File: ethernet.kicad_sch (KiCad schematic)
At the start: 3 parts, among them U1 MCIMX6Y2DVM09AB

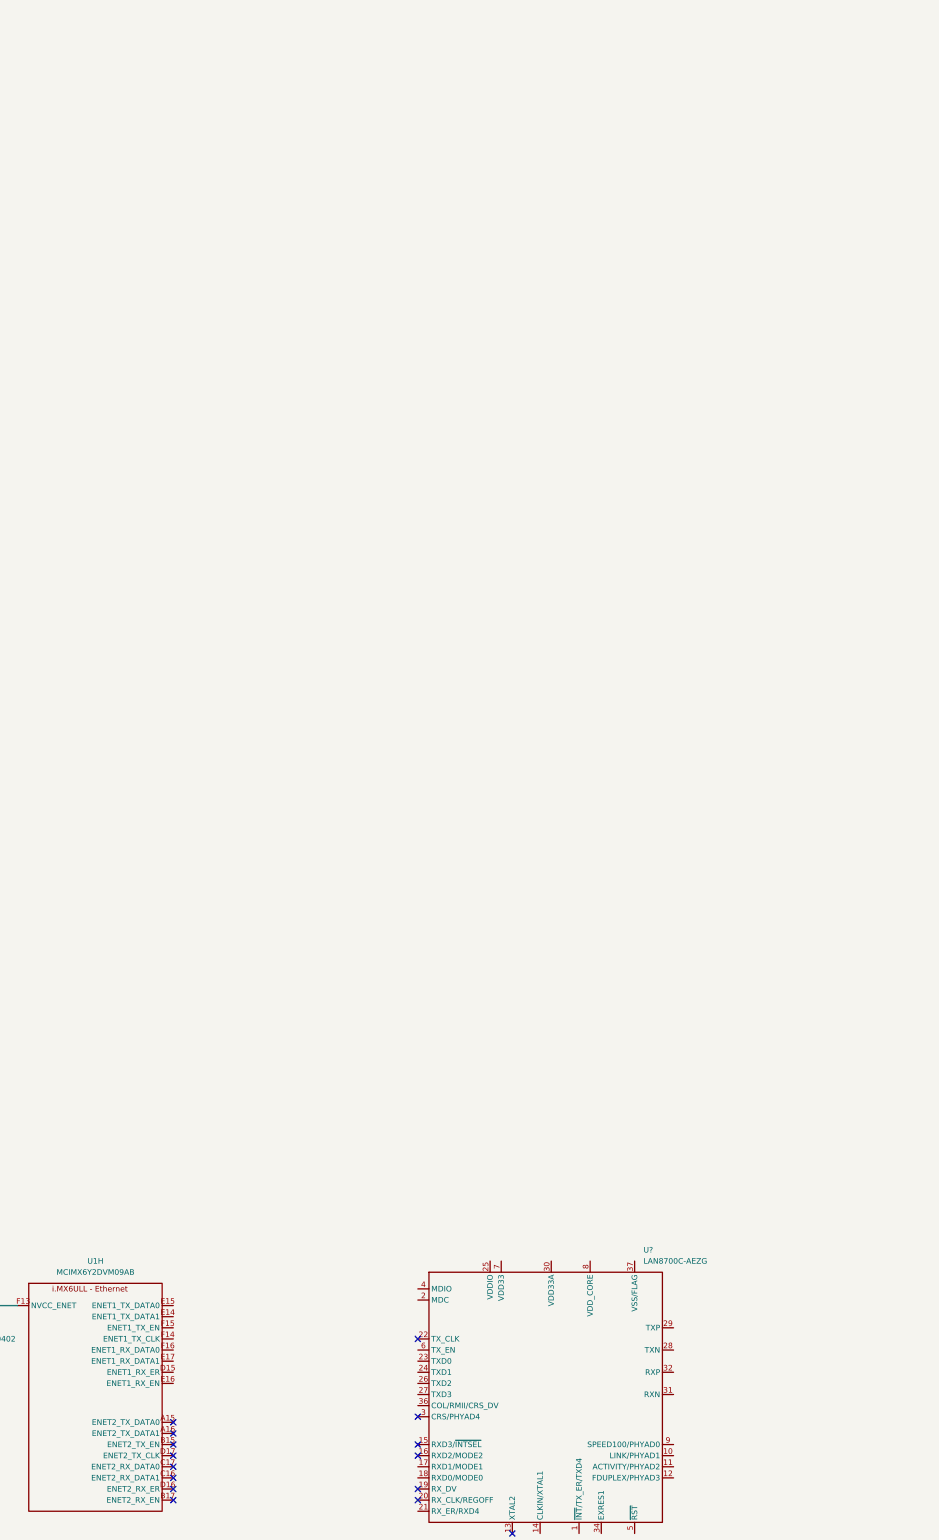
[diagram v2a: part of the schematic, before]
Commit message: H1102 symbol
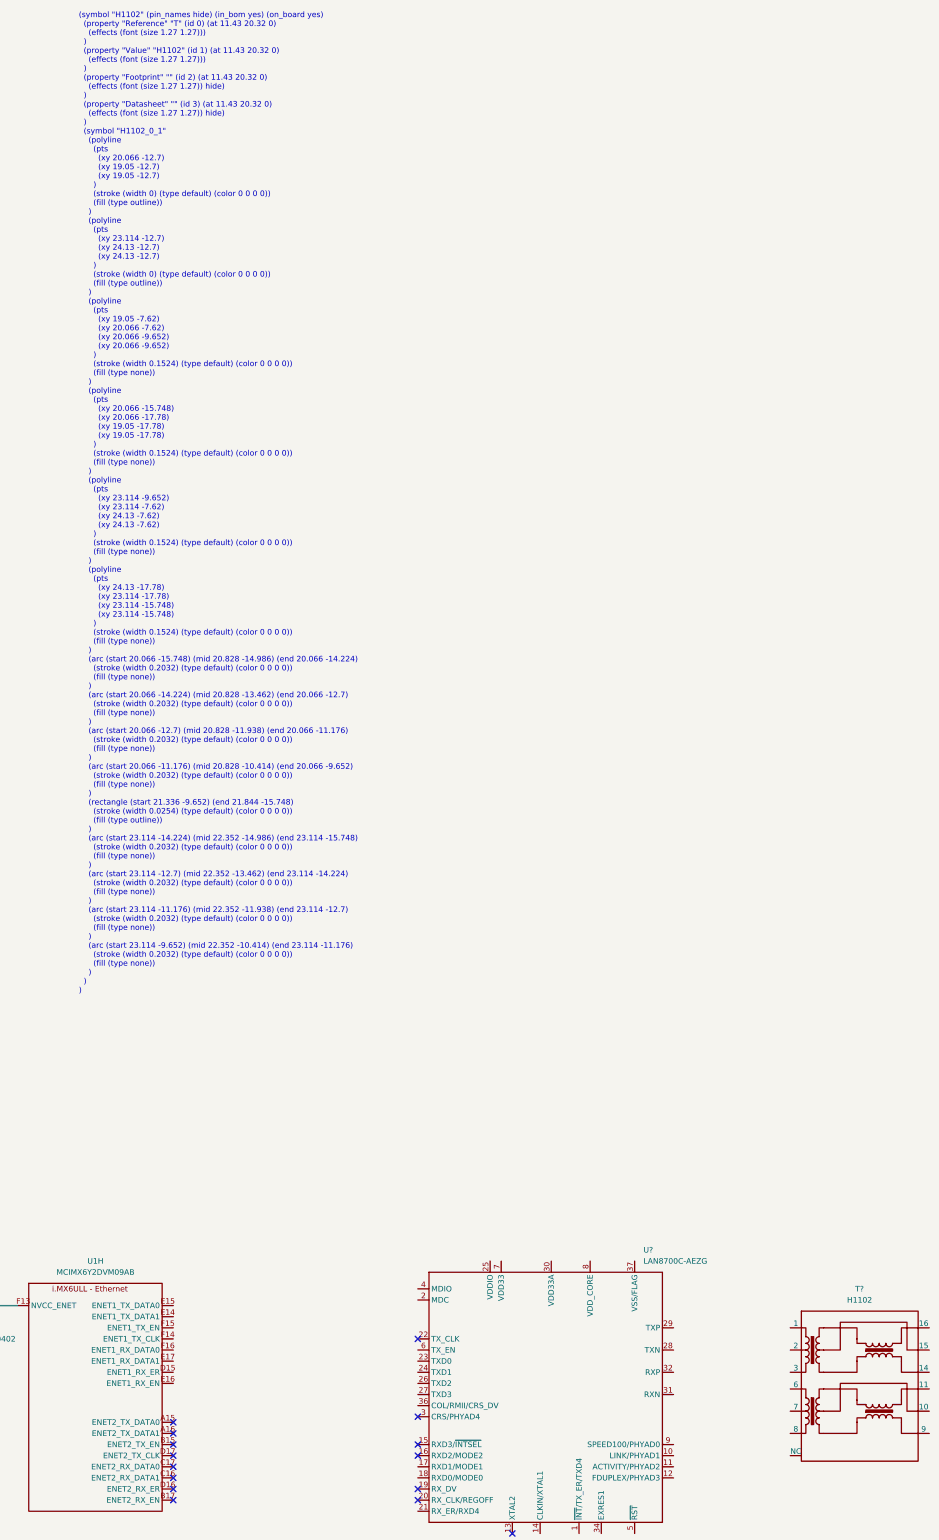
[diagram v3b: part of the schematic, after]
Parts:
- added T?: H1102, symbol catfood:H1102
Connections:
- new net: T?.12 (NC), T?.13 (NC), T?.4 (NC), T?.5 (NC)
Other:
- note added: "(symbol "H1102" (pin_names hide) (in_bom yes) (on_board yes) (property "Reference" "T" (id 0) (at 11.43 20.32 0) (effects (font (size 1.27 1.27))) ) (property "Value" "H1102" (id 1) (at 11.43 20.32 0) (effects (font (size 1.27 1.27))) ) (property "Footprint" "" (id 2) (at 11.43 20.32 0) (effects (font (size 1.27 1.27)) hide) ) (property "Datasheet" "" (id 3) (at 11.43 20.32 0) (effects (font (siz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"
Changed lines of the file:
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@@
     (stroke (width 0) (type default) (color 0 0 0 0))
+  )
+  (text "(symbol \"H1102\" (pin_names hide) (in_bom yes) (on_board yes)\n  (property \"Reference\" \"T\" (id 0) (at 11.43 20.32 0)\n    (effects (font (size 1.27 1.27)))\n  )\n  (property \"Value\" \"H1102\" (id 1) (at 11.43 20.32 0)\n    (effects (font (size 1.27 1.27)))\n  )\n  (property \"Footprint\" \"\" (id 2) (at 11.43 20.32 0)\n    (effects (font (size 1.27 1.27)) hide)\n  )\n  (property \"Datasheet\" \"\" (id 3) (at 11.43 20.32 0)\n    (effects (font (size 1.27 1.27)) hide)\n  )\n  (symbol \"H1102_0_1\"\n    (polyline\n      (pts\n        (xy 20.066 -12.7)\n        (xy 19.05 -12.7)\n        (xy 19.05 -12.7)\n      )\n      (stroke (width 0) (type default) (color 0 0 0 0))\n      (fill (type outline))\n    )\n    (polyline\n      (pts\n        (xy 23.114 -12.7)\n        (xy 24.13 -12.7)\n        (xy 24.13 -12.7)\n      )\n      (stroke (width 0) (type default) (color 0 0 0 0))\n      (fill (type outline))\n    )\n    (polyline\n      (pts\n        (xy 19.05 -7.62)\n        (xy 20.066 -7.62)\n        (xy 20.066 -9.652)\n        (xy 20.066 -9.652)\n      )\n      (stroke (width 0.1524) (type default) (color 0 0 0 0))\n      (fill (type none))\n    )\n    (polyline\n      (pts\n        (xy 20.066 -15.748)\n        (xy 20.066 -17.78)\n        (xy 19.05 -17.78)\n        (xy 19.05 -17.78)\n      )\n      (stroke (width 0.1524) (type default) (color 0 0 0 0))\n      (fill (type none))\n    )\n    (polyline\n      (pts\n        (xy 23.114 -9.652)\n        (xy 23.114 -7.62)\n        (xy 24.13 -7.62)\n        (xy 24.13 -7.62)\n      )\n      (stroke (width 0.1524) (type default) (color 0 0 0 0))\n      (fill (type none))\n    )\n    (polyline\n      (pts\n        (xy 24.13 -17.78)\n        (xy 23.114 -17.78)\n        (xy 23.114 -15.748)\n        (xy 23.114 -15.748)\n      )\n      (stroke (width 0.1524) (type default) (color 0 0 0 0))\n      (fill (type none))\n    )\n    (arc (start 20.066 -15.748) (mid 20.828 -14.986) (end 20.066 -14.224)\n      (stroke (width 0.2032) (type default) (color 0 0 0 0))\n      (fill (type none))\n    )\n    (arc (start 20.066 -14.224) (mid 20.828 -13.462) (end 20.066 -12.7)\n      (stroke (width 0.2032) (type default) (color 0 0 0 0))\n      (fill (type none))\n    )\n    (arc (start 20.066 -12.7) (mid 20.828 -11.938) (end 20.066 -11.176)\n      (stroke (width 0.2032) (type default) (color 0 0 0 0))\n      (fill (type none))\n    )\n    (arc (start 20.066 -11.176) (mid 20.828 -10.414) (end 20.066 -9.652)\n      (stroke (width 0.2032) (type default) (color 0 0 0 0))\n      (fill (type none))\n    )\n    (rectangle (start 21.336 -9.652) (end 21.844 -15.748)\n      (stroke (width 0.0254) (type default) (color 0 0 0 0))\n      (fill (type outline))\n    )\n    (arc (start 23.114 -14.224) (mid 22.352 -14.986) (end 23.114 -15.748)\n      (stroke (width 0.2032) (type default) (color 0 0 0 0))\n      (fill (type none))\n    )\n    (arc (start 23.114 -12.7) (mid 22.352 -13.462) (end 23.114 -14.224)\n      (stroke (width 0.2032) (type default) (color 0 0 0 0))\n      (fill (type none))\n    )\n    (arc (start 23.114 -11.176) (mid 22.352 -11.938) (end 23.114 -12.7)\n      (stroke (width 0.2032) (type default) (color 0 0 0 0))\n      (fill (type none))\n    )\n    (arc (start 23.114 -9.652) (mid 22.352 -10.414) (end 23.114 -11.176)\n      (stroke (width 0.2032) (type default) (color 0 0 0 0))\n      (fill (type none))\n    )\n  )\n)\n"
+    (at 45.72 15.24 0)
+    (effects (font (size 1.27 1.27)) (justify left bottom))
+  )
+  (symbol (lib_id "catfood:H1102") (at 191.77 83.82 0) (unit 1)
+    (in_bom yes) (on_board yes) (fields_autoplaced)
+    (property "Reference" "T?" (id 0) (at 224.1169 82.55 0))
+    (property "Value" "H1102" (id 1) (at 224.1169 85.09 0))
+    (property "Footprint" "" (id 2) (at 218.44 83.82 0)
+      (effects (font (size 1.27 1.27)) hide)
+    )
+    (property "Datasheet" "" (id 3) (at 218.44 83.82 0)
+      (effects (font (size 1.27 1.27)) hide)
+    )
+    (pin "1")
+    (pin "10")
+    (pin "11")
+    (pin "12")
+    (pin "13")
+    (pin "14")
+    (pin "15")
+    (pin "16")
+    (pin "2")
+    (pin "3")
+    (pin "4")
+    (pin "5")
+    (pin "6")
+    (pin "7")
+    (pin "8")
+    (pin "9")
   )
   (symbol (lib_id "Device:C_Small") (at 17.78 92.71 0) (unit 1)

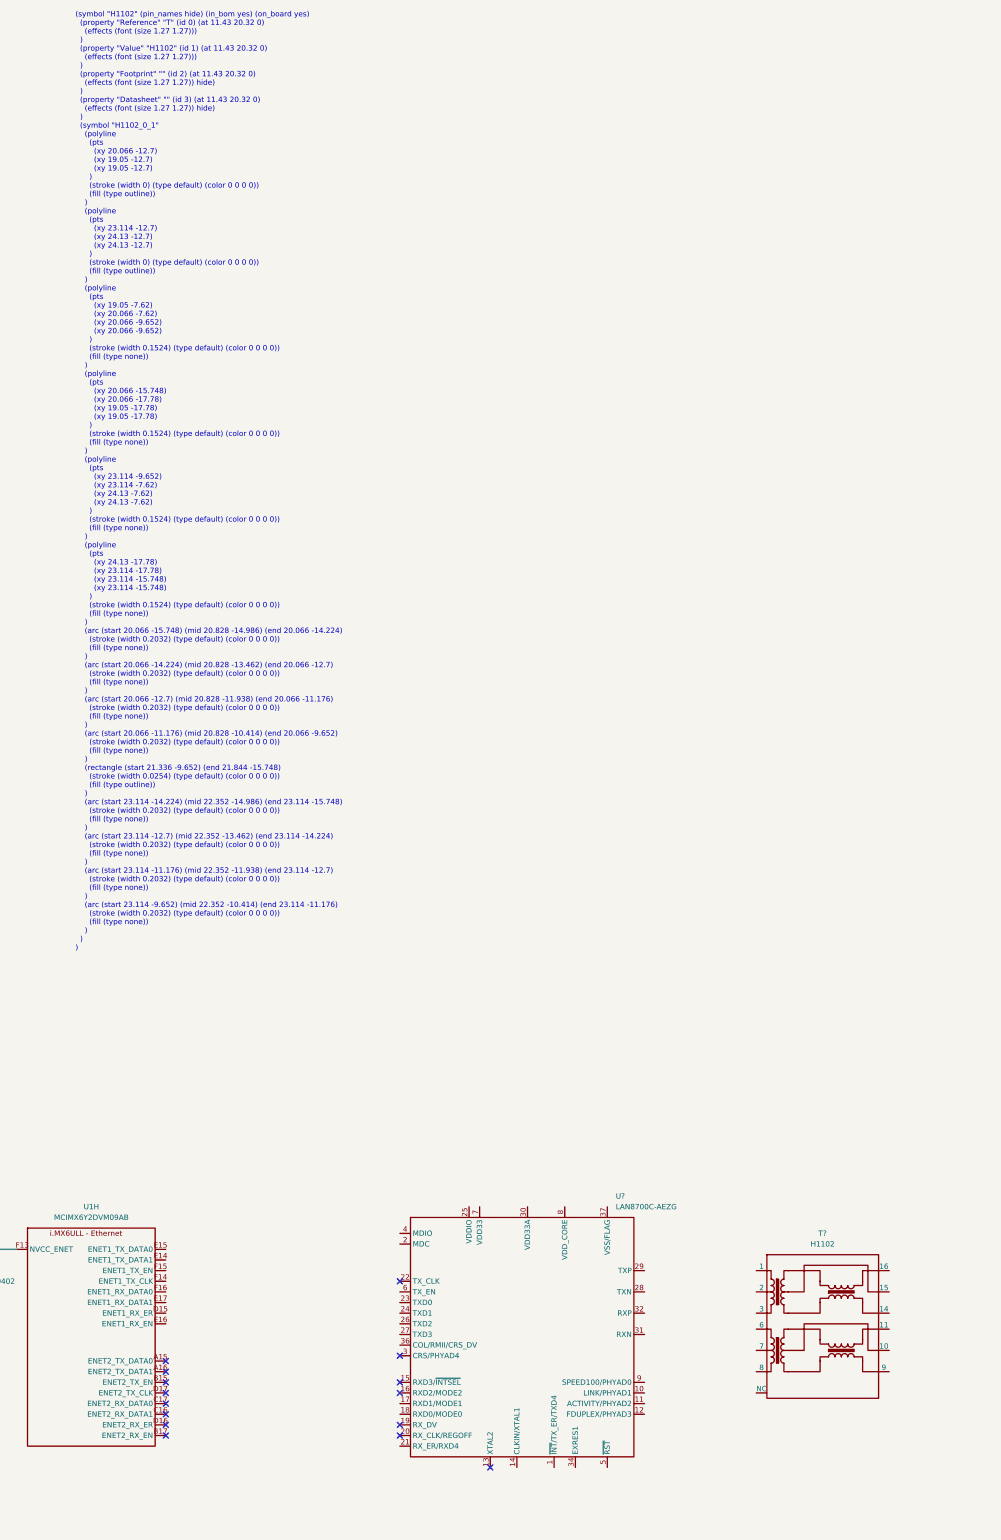
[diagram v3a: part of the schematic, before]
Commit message: TE-1888250-1 symbol
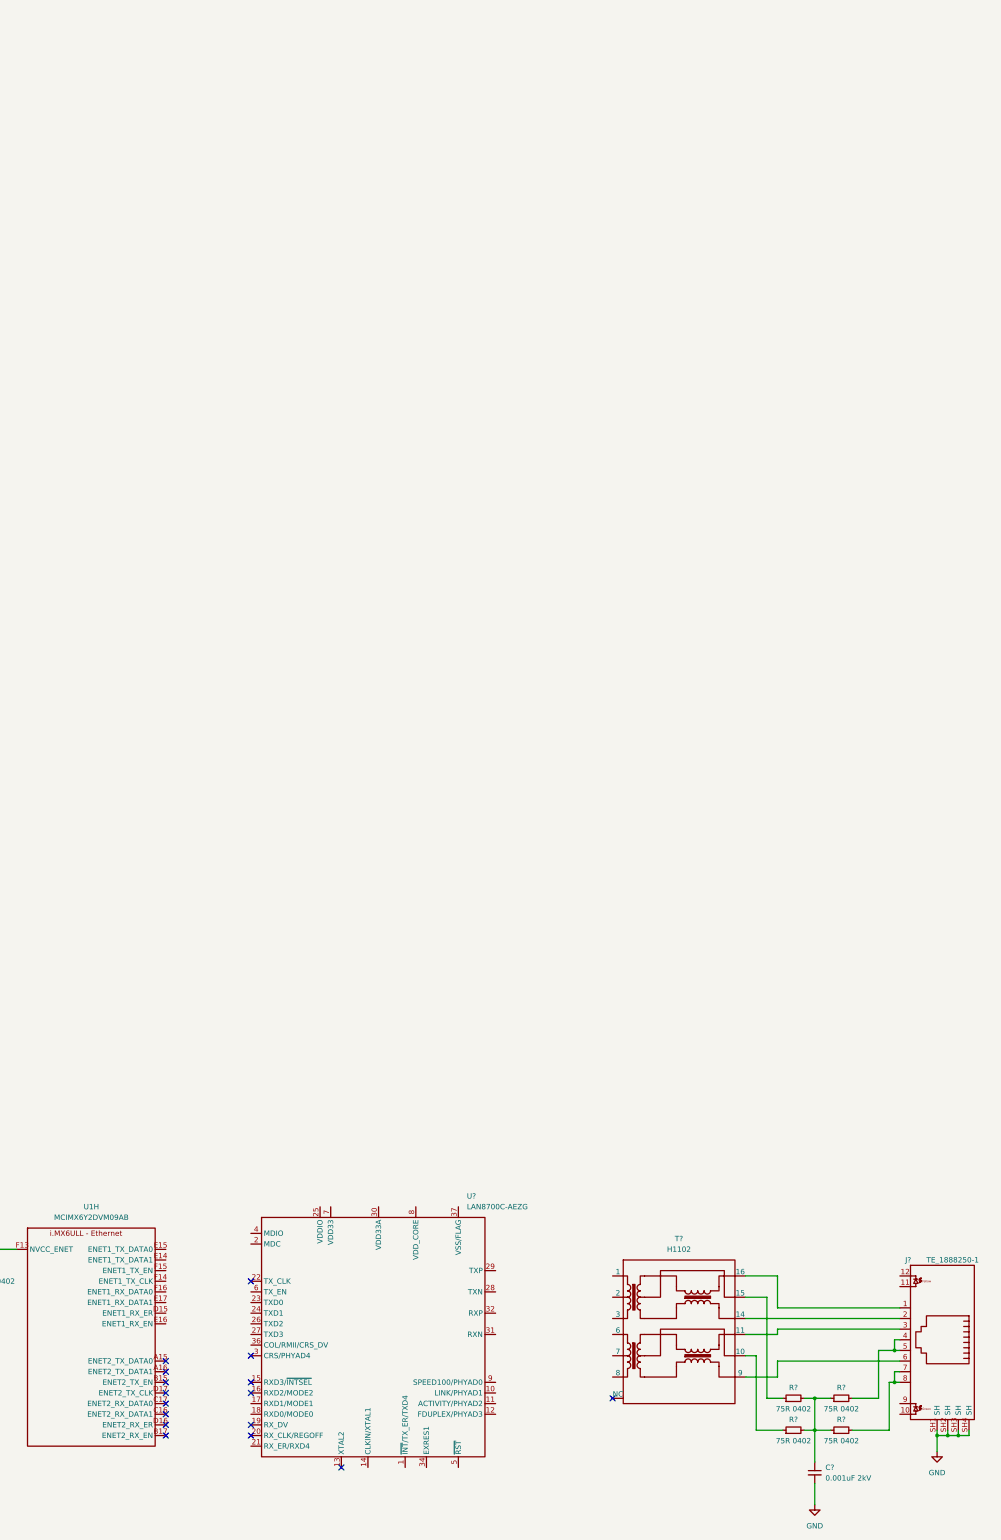
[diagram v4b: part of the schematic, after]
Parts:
- added C?: 0.001uF 2kV, symbol Device:C_Small
- added J?: TE_1888250-1, symbol catfood:TE_1888250-1
- added R? (x4): 75R 0402, symbol Device:R_Small
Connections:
- net GND: now also C?.2, J?.SH1 (SH), J?.SH2 (SH), J?.SH3 (SH), J?.SH4 (SH)
- net at T?.10: now also R?.1
- net at T?.11: now also J?.3
- net at T?.14: now also J?.2
- net at T?.15: now also R?.1
- net at T?.16: now also J?.1
- net at T?.9: now also J?.6
- new net: C?.1, R?.1, R?.1, R?.2, R?.2
- new net: J?.7, J?.8, R?.2
- new net: J?.4, J?.5, R?.2
- no-connect marks 15 -> 16
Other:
- note removed: "(symbol "H1102" (pin_names hide) (in_bom yes) (on_board yes) (property "Reference" "T" (id 0) (at 11.43 20.32 0) (effects (font (size 1.27 1.27))) ) (property "Value" "H1102" (id 1) (at 11.43 20.32 0) (effects (font (size 1.27 1.27))) ) (property "Footprint" "" (id 2) (at 11.43 20.32 0) (effects (font (size 1.27 1.27)) hide) ) (property "Datasheet" "" (id 3) (at 11.43 20.32 0) (effects (font (siz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"
- moved on the sheet: T?, U?

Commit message: Ethernet schematic
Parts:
- added C?: 18pF 0402, symbol Device:C_Small
- added C?: 0.022uF 0402 50V, symbol Device:C_Small
- added C? (x7): 0.1uF 0402, symbol Device:C_Small
- added C?: 4.7uF 0603, symbol Device:C_Small
- added FB?: FERRITE 33 0402 500mA, symbol Device:FerriteBead_Small
- added R?: 12.4k 0402 1%, symbol Device:R_Small
- added R? (x3): 10k 0402, symbol Device:R_Small
- added R? (x4): 49R9 0402, symbol Device:R_Small
- added R?: 1.5k 0402, symbol Device:R_Small
- added R? (x2): 330R 0402, symbol Device:R_Small
- added R? (x2): 10R 0402, symbol Device:R_Small
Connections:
- net GND: now also U?.26 (TXD2), U?.27 (TXD3), U?.37 (VSS/FLAG), C?.2, C?.2, C?.2, C?.2, C?.2, C?.2, C?.2, C?.2, C?.2, C?.2, R?.2
- net VDD_3V3: now also J?.10, J?.11, U?.25 (VDDIO), U?.7 (VDD33), C?.1, C?.1, FB?.1, R?.1, R?.1, R?.1, R?.1
- net ETH_TX_P: now reaches T?.1
- net ETH_TX_P: now also U?.29 (TXP), R?.2
- net at T?.2: now also T?.7, C?.1, R?.2
- net ETH_TX_N: now reaches T?.3
- net ETH_TX_N: now also U?.28 (TXN), R?.2
- net ETH_RX_P: now reaches T?.6
- net ETH_RX_P: now also U?.32 (RXP), R?.2
- net ETH_RX_N: now reaches T?.8
- net ETH_RX_N: now also U?.31 (RXN), R?.2
- net ENET_RXER: now reaches U1.D15 (ENET1_RX_ER)
- net ENET_RXER: now also U?.21 (RX_ER/RXD4)
- net ENET_TXD1: now reaches U1.E14 (ENET1_TX_DATA1)
- net ENET_TXD1: now also U?.24 (TXD1)
- net ENET_TXD0: now reaches U1.E15 (ENET1_TX_DATA0)
- net ENET_TXD0: now also U?.23 (TXD0)
- net ENET_CRSDV: now reaches U1.E16 (ENET1_RX_EN)
- net ENET_CRSDV: now also U?.36 (COL/RMII/CRS_DV), R?.2
- net ENET_RXD1: now reaches U1.E17 (ENET1_RX_DATA1)
- net ENET_RXD1: now also U?.17 (RXD1/MODE1)
- net ENET_REF_CLK: now reaches U1.F14 (ENET1_TX_CLK)
- net ENET_REF_CLK: now also R?.1
- net ENET_TXEN: now reaches U1.F15 (ENET1_TX_EN)
- net ENET_TXEN: now also U?.6 (TX_EN)
- net ENET_RXD0: now reaches U1.F16 (ENET1_RX_DATA0)
- net ENET_RXD0: now also U?.18 (RXD0/MODE0)
- net ~{ENET1_INT}: now reaches U?.1 (~{INT}/TX_ER/TXD4)
- net ~{ENET1_INT}: now also R?.2
- net LINKLED: now reaches U?.10 (LINK/PHYAD1)
- net LINKLED: now also R?.1
- net ACTIVITYLED: now reaches U?.11 (ACTIVITY/PHYAD2)
- net ACTIVITYLED: now also R?.1
- net ENET_REF_CLK_TRM: now reaches U?.14 (CLKIN/XTAL1)
- net ENET_REF_CLK_TRM: now also C?.1, R?.2
- net ENET_MDC: now reaches U?.2 (MDC)
- net VETH_3V3: now reaches U?.30 (VDD33A), U?.33 (VDD33A), U?.35 (VDD33A)
- net VETH_3V3: now also C?.1, C?.1, C?.1, FB?.2, R?.1, R?.1, R?.1, R?.1, R?.1
- net at U?.34 (EXRES1): now also R?.1
- net ENET_MDIO: now reaches U?.4 (MDIO)
- net ENET_MDIO: now also R?.2
- net ~{ENET1_RST}: now reaches U?.5 (~{RST})
- net ~{ENET1_RST}: now also C?.1, R?.2
- net at U?.8 (VDD_CORE): now also C?.1, C?.1
- net at J?.12: now also R?.2
- net at J?.9: now also R?.2
- no-connect marks 16 -> 18
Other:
- note added: "COL/RMII/CRS_DV pulled up for RMII mode"
- note added: "~{INTSEL} floating -> pin 1 is ~{INT}"
- moved on the sheet: C?, J?, R?, T?, U1H, U?

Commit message: USB, GPIO
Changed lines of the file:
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@@
     (effects (font (size 1.27 1.27)) (justify left bottom))
   )
-  (hierarchical_label "ENET_MDIO" (shape input) (at 118.11 118.11 180)
+  (hierarchical_label "ENET_MDIO" (shape bidirectional) (at 118.11 118.11 180)
     (effects (font (size 1.27 1.27)) (justify right))
   )
